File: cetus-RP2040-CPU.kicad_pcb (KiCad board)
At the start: 4 copper layers, 44.3 x 50.8 mm, 38 parts, among them J1 Conn_01x03, J2 Conn_01x02, J3 Conn_01x02, J4 Conn_02x03_Odd_Even, U2 W25Q128JVS, U3 RP2040, Y1 ABLS-12.000MHZ-B4-T, Y2 X322516MLB4SI

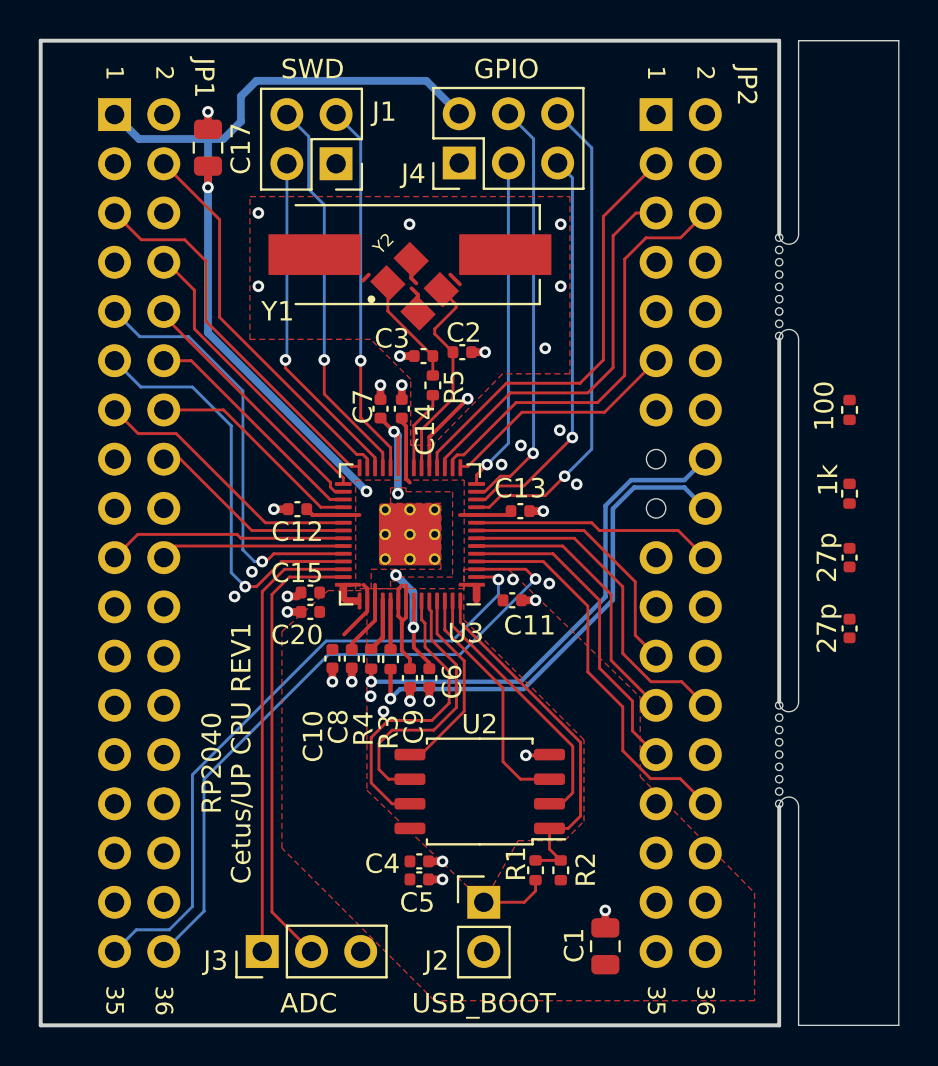
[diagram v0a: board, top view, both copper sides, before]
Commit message: Remove spare components and break-off tab
Also, fix PCB DRC errors/warnings:

- Create a custom symbol for header to match footprint with missing pads

- Create footprints for flash and crystal which have 3D models
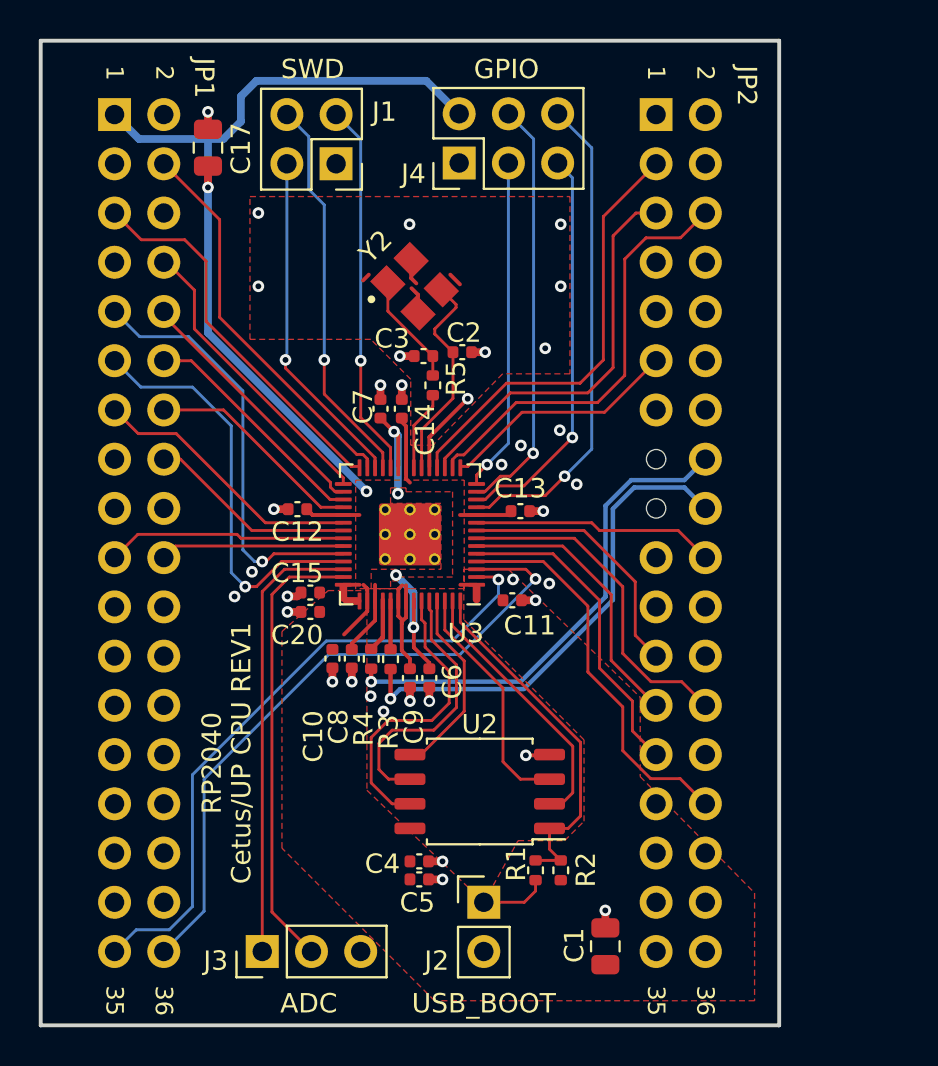
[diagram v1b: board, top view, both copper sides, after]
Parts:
- removed C16, C18: 27p, Capacitor_SMD:C_0402_1005Metric
- removed R6: 100, Resistor_SMD:R_0402_1005Metric
- removed R7: 1k, Resistor_SMD:R_0402_1005Metric
- removed Y1: ABLS-12.000MHZ-B4-T, RP2040_minimal:Crystal_SMD_HC49-US
- removed mouse-bite-2mm-slot (x2): VAL**, RP2040_minimal:mouse-bite-1mm-slot_singlesided
- U2: footprint Package_SO:SOIC-8_5.23x5.23mm_P1.27mm -> custom:SOIC-8_5.23x5.23mm_P1.27mm+model
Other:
- board size 44.3 x 50.8 mm -> 38.1 x 50.8 mm

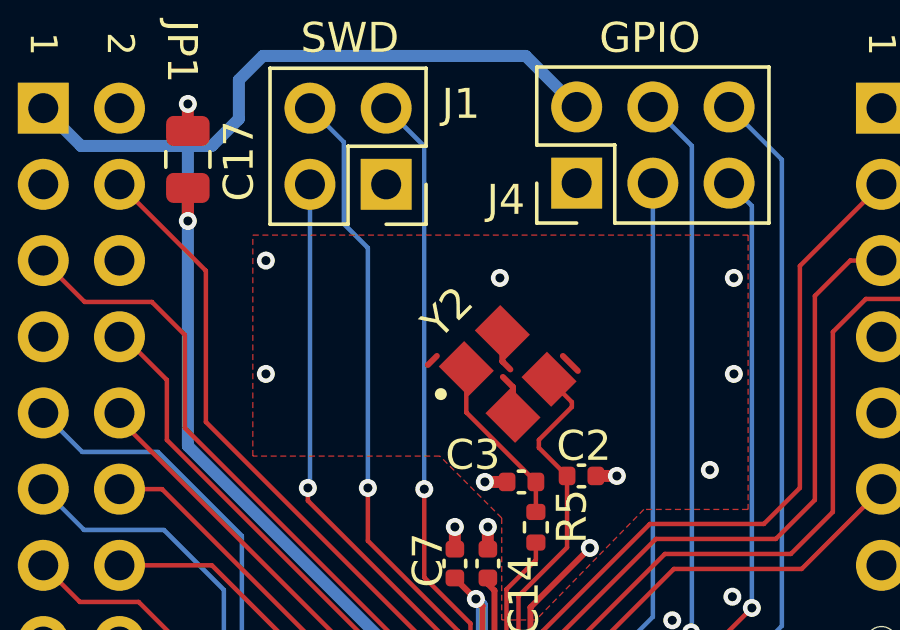
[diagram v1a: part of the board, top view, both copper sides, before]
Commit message: Fix silkscreen crystal designation text size
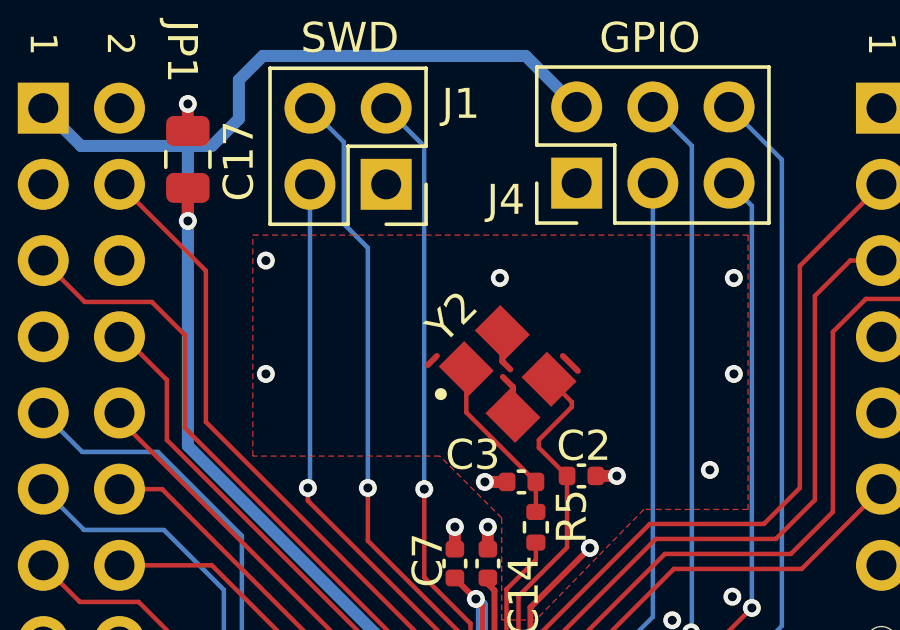
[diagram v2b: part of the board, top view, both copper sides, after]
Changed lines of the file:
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@@
     (property "Sheetname" "")
     (attr smd)
-    (fp_text reference "Y2" (at 0.028284 -2.870854 45) (layer "F.SilkS")
+    (fp_text reference "Y2" (at 0.032 -2.6564 45) (layer "F.SilkS")
         (effects (font (size 1 1) (thickness 0.15)))
     )
@@
       (net 1 "GND") (pinfunction "Pin_26") (pintype "passive"))
     (pad "27" thru_hole oval (at 2.54 -33.02 180) (size 1.7 1.7) (drill 1) (layers "*.Cu" "*.Mask")
-      (net 34 "unconnected-(JP1-Pin_27-Pad27)") (pinfunction "Pin_27") (pintype "passive"))
+      (net 34 "unconnected-(JP1-Pin_27-Pad27)") (pinfunction "Pin_27") (pintype "passive+no_connect"))
     (pad "28" thru_hole oval (at 0 -33.02 180) (size 1.7 1.7) (drill 1) (layers "*.Cu" "*.Mask")
       (net 35 "unconnected-(JP1-Pin_28-Pad28)") (pinfunction "Pin_28") (pintype "passive+no_connect"))
     (pad "29" thru_hole oval (at 2.54 -35.56 180) (size 1.7 1.7) (drill 1) (layers "*.Cu" "*.Mask")
-      (net 40 "unconnected-(JP1-Pin_29-Pad29)") (pinfunction "Pin_29") (pintype "passive"))
+      (net 40 "unconnected-(JP1-Pin_29-Pad29)") (pinfunction "Pin_29") (pintype "passive+no_connect"))
     (pad "30" thru_hole oval (at 0 -35.56 180) (size 1.7 1.7) (drill 1) (layers "*.Cu" "*.Mask")
       (net 46 "unconnected-(JP1-Pin_30-Pad30)") (pinfunction "Pin_30") (pintype "passive+no_connect"))
     (pad "31" thru_hole oval (at 2.54 -38.1 180) (size 1.7 1.7) (drill 1) (layers "*.Cu" "*.Mask")
-      (net 48 "unconnected-(JP1-Pin_31-Pad31)") (pinfunction "Pin_31") (pintype "passive"))
+      (net 48 "unconnected-(JP1-Pin_31-Pad31)") (pinfunction "Pin_31") (pintype "passive+no_connect"))
     (pad "32" thru_hole oval (at 0 -38.1 180) (size 1.7 1.7) (drill 1) (layers "*.Cu" "*.Mask")
       (net 49 "unconnected-(JP1-Pin_32-Pad32)") (pinfunction "Pin_32") (pintype "passive+no_connect"))
     (pad "33" thru_hole oval (at 2.54 -40.64 180) (size 1.7 1.7) (drill 1) (layers "*.Cu" "*.Mask")
-      (net 50 "unconnected-(JP1-Pin_33-Pad33)") (pinfunction "Pin_33") (pintype "passive"))
+      (net 50 "unconnected-(JP1-Pin_33-Pad33)") (pinfunction "Pin_33") (pintype "passive+no_connect"))
     (pad "34" thru_hole oval (at 0 -40.64 180) (size 1.7 1.7) (drill 1) (layers "*.Cu" "*.Mask")
       (net 51 "unconnected-(JP1-Pin_34-Pad34)") (pinfunction "Pin_34") (pintype "passive+no_connect"))

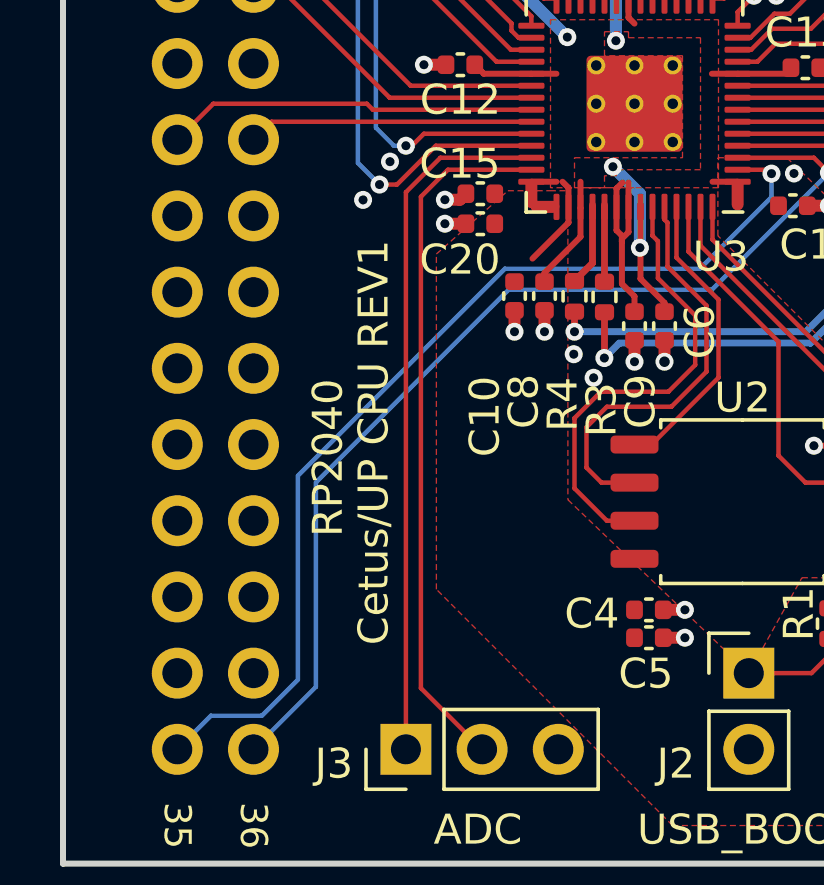
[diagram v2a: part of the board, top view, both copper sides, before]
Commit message: Update README to rev2
- Fix crystal footprint: add 3D model
- Generate new 3D view
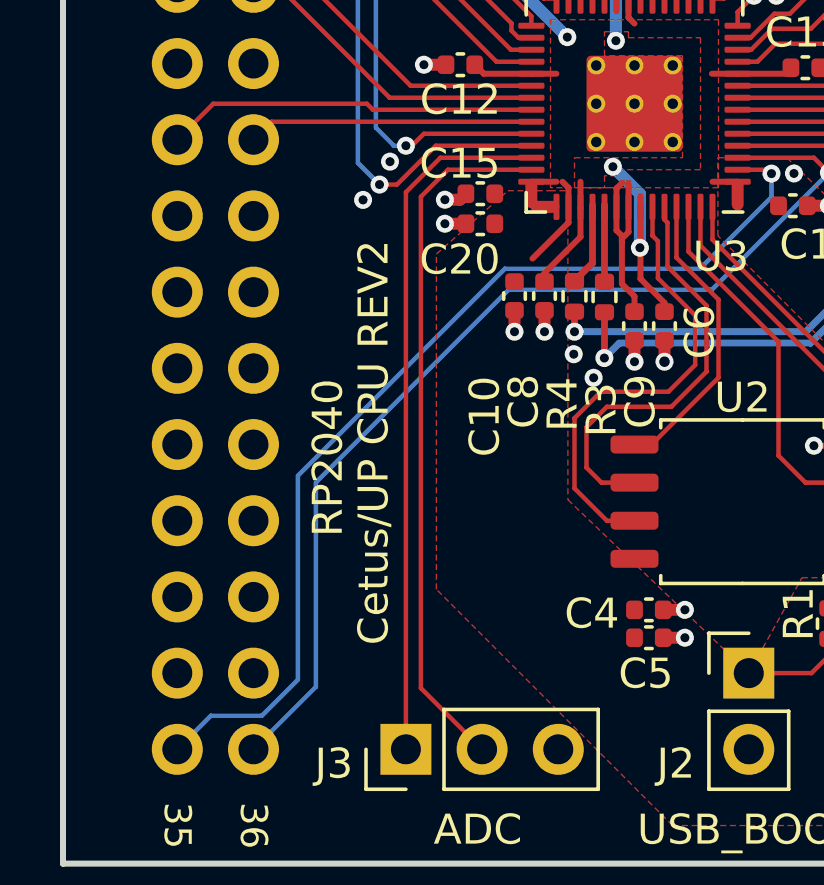
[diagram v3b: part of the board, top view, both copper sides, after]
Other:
- board text added: "Cetus/UP CPU REV2"
- board text removed: "Cetus/UP CPU REV1"
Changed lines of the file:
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@@
     (pad "4" smd rect (at 0.85 -1.1 45) (size 1.2 1.4) (layers "F.Cu" "F.Paste" "F.Mask")
       (net 1 "GND") (pintype "power_in"))
+    (model ":KICAD7_3DMODEL_DIR:Crystal.3dshapes/Crystal_SMD_3225-4Pin_3.2x2.5mm.wrl"
+      (offset (xyz 0 0 0))
+      (scale (xyz 1 1 1))
+      (rotate (xyz 0 0 90))
+    )
   )
   (footprint "RP2040_minimal:PinHeader_2x18_P2.54mm_Vertical_backside" (layer "B.Cu")
@@
     (effects (font (size 1 1) (thickness 0.15)))
   )
-  (gr_text "Cetus/UP CPU REV1" (at 151.324 111.692 90) (layer "F.SilkS")
-    (effects (font (size 1 1) (thickness 0.15)))
-  )
+  (gr_text "Cetus/UP CPU REV2" (at 151.324 111.692 90) (layer "F.SilkS")
+    (effects (font (size 1 1) (thickness 0.15)))
+  )
